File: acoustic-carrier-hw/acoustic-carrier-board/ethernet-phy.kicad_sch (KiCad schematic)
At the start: 49 parts, among them J1201 HR911130A, U1201 KSZ9031RN, Y1201 25MHz

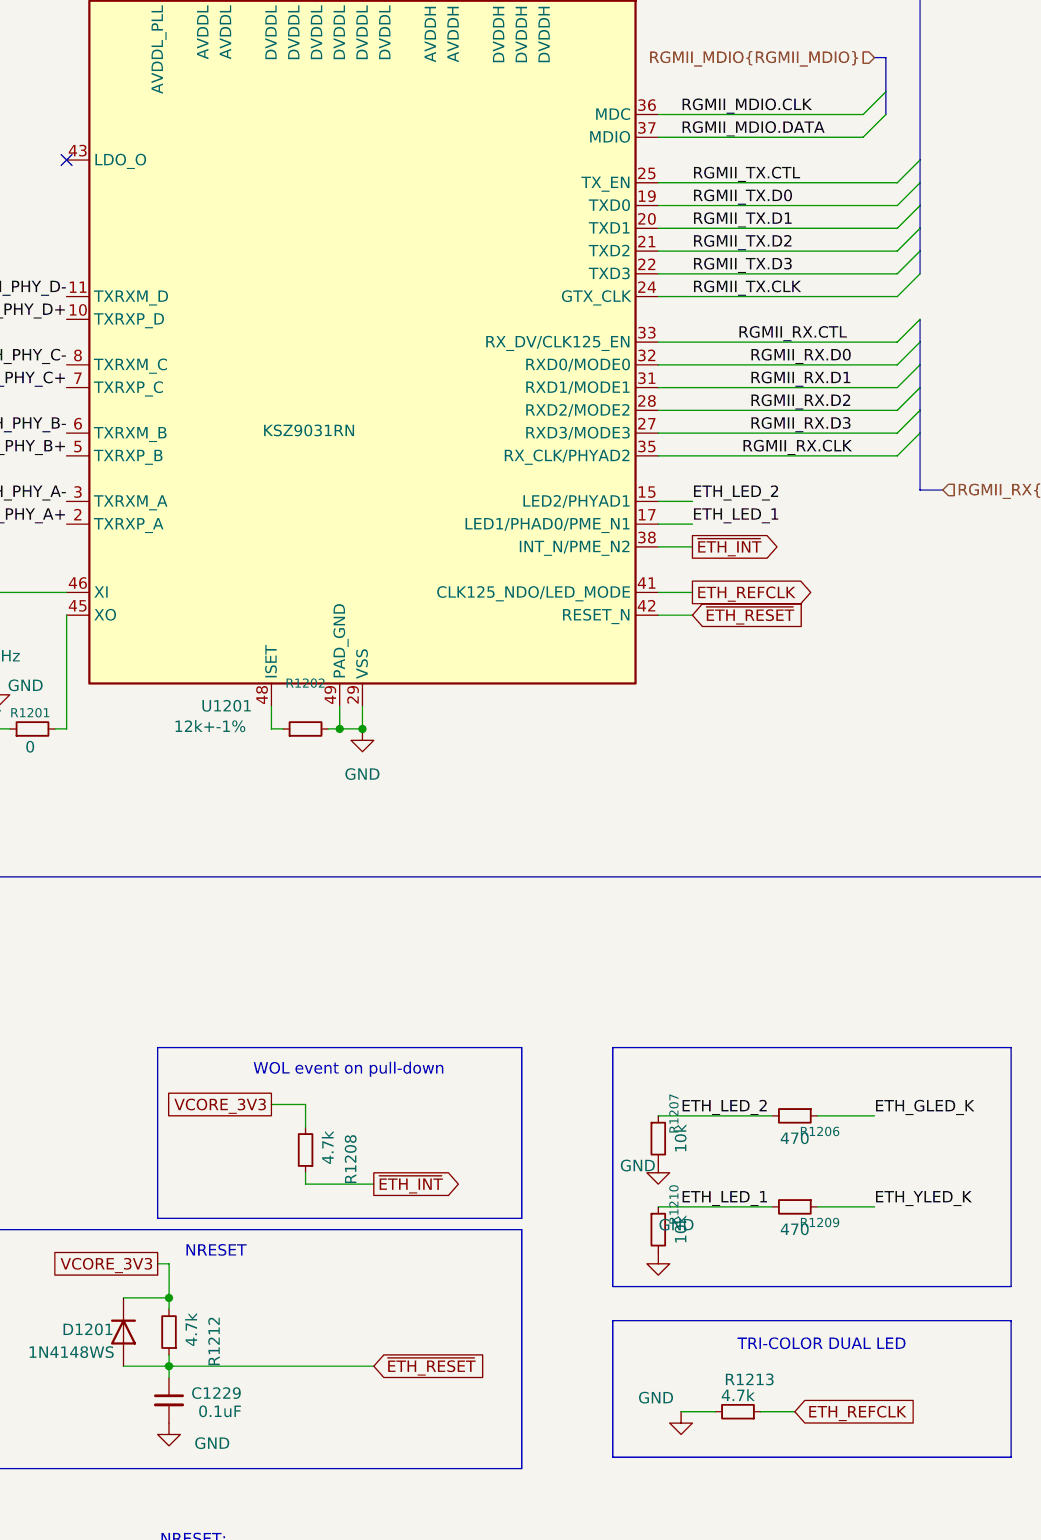
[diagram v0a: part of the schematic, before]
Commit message: [carrier] finished for production (next) reroute the LPDDR3, with appropriate CMD-CTRL bus delays, and change banks for command-control
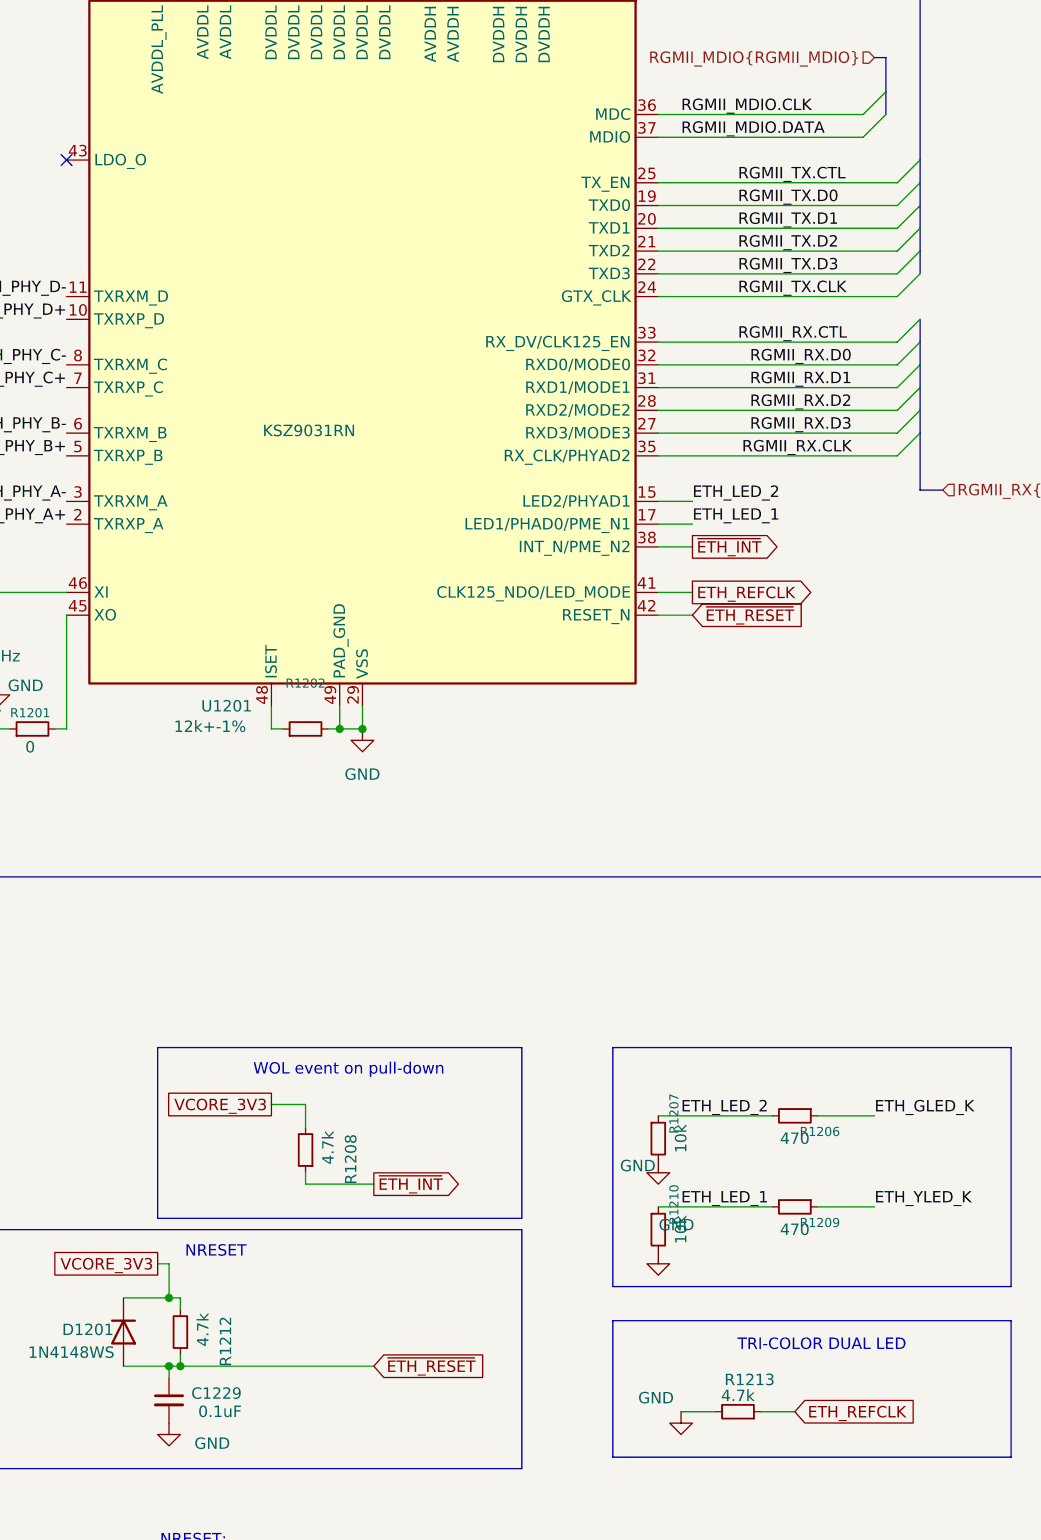
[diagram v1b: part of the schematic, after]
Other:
- moved on the sheet: R1212
